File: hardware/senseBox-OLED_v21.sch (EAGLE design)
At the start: 28 parts, among them IC2 VREG-TS9011-3V3, IC4 MAX8XX-809R, J1 JUMPER2-0402-NC, J2 JST4-B4B-PH-SM4-TB, T3 BSS138PS, X1 PASSER-07, X2 PASSER-07, X3 PASSER-07, X4 PASSER-07

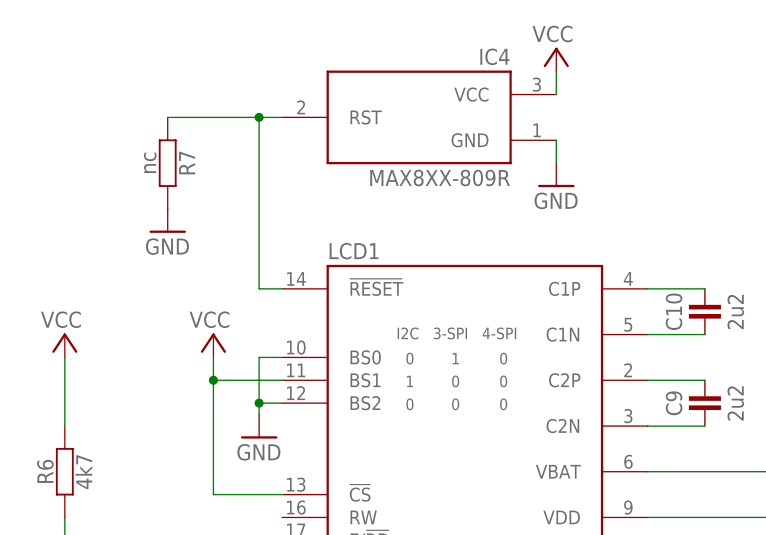
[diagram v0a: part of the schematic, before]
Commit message: updated schematics
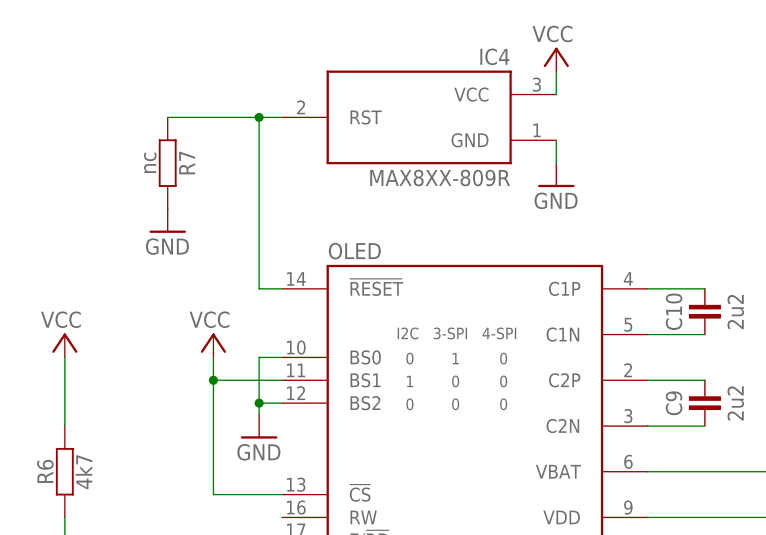
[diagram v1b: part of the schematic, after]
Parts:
- renumbered LCD1 to OLED
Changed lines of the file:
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@@
 <part name="C4" library="we-rcl" deviceset="CAPACITOR" device="-0402" value="100n"/>
 <part name="C1" library="we-rcl" deviceset="CAPACITOR" device="-0402" value="100n"/>
-<part name="LCD1" library="we-opto" deviceset="UG2864HSWEG01" device="-B"/>
+<part name="OLED" library="we-opto" deviceset="UG2864HSWEG01" device="-B"/>
 <part name="GND7" library="supply1" deviceset="GND" device=""/>
 <part name="R6" library="we-rcl" deviceset="RESISTOR" device="-0402" value="4k7"/>
@@
 <instance part="C4" gate="C" x="139.7" y="19.05" rot="R90"/>
 <instance part="C1" gate="C" x="86.36" y="19.05" rot="R90"/>
-<instance part="LCD1" gate="LCD" x="113.03" y="111.76"/>
+<instance part="OLED" gate="LCD" x="113.03" y="111.76"/>
 <instance part="GND7" gate="1" x="90.17" y="120.65"/>
 <instance part="R6" gate="R" x="68.58" y="116.84" rot="R90"/>
@@
 </segment>
 <segment>
-<pinref part="LCD1" gate="LCD" pin="BS2"/>
+<pinref part="OLED" gate="LCD" pin="BS2"/>
 <wire x1="92.71" y1="124.46" x2="90.17" y2="124.46" width="0.1524" layer="91"/>
 <wire x1="92.71" y1="129.54" x2="90.17" y2="129.54" width="0.1524" layer="91"/>
@@
 <wire x1="90.17" y1="124.46" x2="90.17" y2="123.19" width="0.1524" layer="91"/>
 <junction x="90.17" y="124.46"/>
-<pinref part="LCD1" gate="LCD" pin="BS0"/>
+<pinref part="OLED" gate="LCD" pin="BS0"/>
 </segment>
 <segment>
@@
 </segment>
 <segment>
-<pinref part="LCD1" gate="LCD" pin="AGND"/>
-<pinref part="LCD1" gate="LCD" pin="GND@3"/>
+<pinref part="OLED" gate="LCD" pin="AGND"/>
+<pinref part="OLED" gate="LCD" pin="GND@3"/>
 <wire x1="133.35" y1="83.82" x2="133.35" y2="86.36" width="0.1524" layer="91"/>
-<pinref part="LCD1" gate="LCD" pin="GND@2"/>
+<pinref part="OLED" gate="LCD" pin="GND@2"/>
 <wire x1="133.35" y1="86.36" x2="133.35" y2="88.9" width="0.1524" layer="91"/>
 <junction x="133.35" y="86.36"/>
-<pinref part="LCD1" gate="LCD" pin="GND@1"/>
+<pinref part="OLED" gate="LCD" pin="GND@1"/>
 <wire x1="133.35" y1="88.9" x2="133.35" y2="91.44" width="0.1524" layer="91"/>
 <junction x="133.35" y="88.9"/>
@@
 </segment>
 <segment>
-<pinref part="LCD1" gate="LCD" pin="!CS"/>
+<pinref part="OLED" gate="LCD" pin="!CS"/>
 <wire x1="92.71" y1="114.3" x2="85.09" y2="114.3" width="0.1524" layer="91"/>
 <wire x1="85.09" y1="114.3" x2="85.09" y2="127" width="0.1524" layer="91"/>
-<pinref part="LCD1" gate="LCD" pin="BS1"/>
+<pinref part="OLED" gate="LCD" pin="BS1"/>
 <wire x1="85.09" y1="127" x2="85.09" y2="129.54" width="0.1524" layer="91"/>
 <wire x1="92.71" y1="127" x2="85.09" y2="127" width="0.1524" layer="91"/>
@@
 </segment>
 <segment>
-<pinref part="LCD1" gate="LCD" pin="VBAT"/>
+<pinref part="OLED" gate="LCD" pin="VBAT"/>
 <pinref part="P+2" gate="VCC" pin="VCC"/>
 <wire x1="133.35" y1="116.84" x2="158.75" y2="116.84" width="0.1524" layer="91"/>
@@
 <wire x1="165.1" y1="97.79" x2="165.1" y2="116.84" width="0.1524" layer="91"/>
 <junction x="165.1" y="116.84"/>
-<pinref part="LCD1" gate="LCD" pin="VDD"/>
+<pinref part="OLED" gate="LCD" pin="VDD"/>
 <pinref part="C7" gate="C" pin="2"/>
 <wire x1="133.35" y1="111.76" x2="158.75" y2="111.76" width="0.1524" layer="91"/>
@@
 <wire x1="90.17" y1="99.06" x2="85.09" y2="99.06" width="0.1524" layer="91"/>
 <label x="85.09" y="99.06" size="1.27" layer="95" rot="R180" xref="yes"/>
-<pinref part="LCD1" gate="LCD" pin="D2/SDA"/>
+<pinref part="OLED" gate="LCD" pin="D2/SDA"/>
 <wire x1="92.71" y1="96.52" x2="90.17" y2="96.52" width="0.1524" layer="91"/>
 <wire x1="90.17" y1="96.52" x2="90.17" y2="99.06" width="0.1524" layer="91"/>
-<pinref part="LCD1" gate="LCD" pin="D1/DIN/SDA"/>
+<pinref part="OLED" gate="LCD" pin="D1/DIN/SDA"/>
 <wire x1="90.17" y1="99.06" x2="92.71" y2="99.06" width="0.1524" layer="91"/>
 <junction x="90.17" y="99.06"/>
@@
 <wire x1="92.71" y1="101.6" x2="85.09" y2="101.6" width="0.1524" layer="91"/>
 <label x="85.09" y="101.6" size="1.27" layer="95" rot="R180" xref="yes"/>
-<pinref part="LCD1" gate="LCD" pin="D0/SCK"/>
+<pinref part="OLED" gate="LCD" pin="D0/SCK"/>
 </segment>
 </net>
 <net name="SA0" class="0">
 <segment>
-<pinref part="LCD1" gate="LCD" pin="DC/I2C_SA0"/>
+<pinref part="OLED" gate="LCD" pin="DC/I2C_SA0"/>
 <wire x1="92.71" y1="106.68" x2="68.58" y2="106.68" width="0.1524" layer="91"/>
 <wire x1="68.58" y1="106.68" x2="68.58" y2="111.76" width="0.1524" layer="91"/>
@@
 <net name="C2N" class="0">
 <segment>
-<pinref part="LCD1" gate="LCD" pin="C2N"/>
+<pinref part="OLED" gate="LCD" pin="C2N"/>
 <wire x1="133.35" y1="121.92" x2="139.7" y2="121.92" width="0.1524" layer="91"/>
 <pinref part="C9" gate="C" pin="1"/>
@@
 <net name="C2P" class="0">
 <segment>
-<pinref part="LCD1" gate="LCD" pin="C2P"/>
+<pinref part="OLED" gate="LCD" pin="C2P"/>
 <wire x1="133.35" y1="127" x2="139.7" y2="127" width="0.1524" layer="91"/>
 <pinref part="C9" gate="C" pin="2"/>
@@
 <net name="C1N" class="0">
 <segment>
-<pinref part="LCD1" gate="LCD" pin="C1N"/>
+<pinref part="OLED" gate="LCD" pin="C1N"/>
 <wire x1="133.35" y1="132.08" x2="139.7" y2="132.08" width="0.1524" layer="91"/>
 <pinref part="C10" gate="C" pin="1"/>
@@
 <net name="C1P" class="0">
 <segment>
-<pinref part="LCD1" gate="LCD" pin="C1P"/>
+<pinref part="OLED" gate="LCD" pin="C1P"/>
 <wire x1="133.35" y1="137.16" x2="139.7" y2="137.16" width="0.1524" layer="91"/>
 <pinref part="C10" gate="C" pin="2"/>
@@
 <net name="IREF" class="0">
 <segment>
-<pinref part="LCD1" gate="LCD" pin="IREF"/>
+<pinref part="OLED" gate="LCD" pin="IREF"/>
 <pinref part="R5" gate="R" pin="1"/>
 <wire x1="138.43" y1="96.52" x2="133.35" y2="96.52" width="0.1524" layer="91"/>
@@
 <net name="VCH" class="0">
 <segment>
-<pinref part="LCD1" gate="LCD" pin="VCOMH"/>
+<pinref part="OLED" gate="LCD" pin="VCOMH"/>
 <pinref part="C5" gate="C" pin="2"/>
 <wire x1="133.35" y1="101.6" x2="146.05" y2="101.6" width="0.1524" layer="91"/>
@@
 <net name="VC" class="0">
 <segment>
-<pinref part="LCD1" gate="LCD" pin="VCC"/>
+<pinref part="OLED" gate="LCD" pin="VCC"/>
 <pinref part="C6" gate="C" pin="2"/>
 <wire x1="133.35" y1="106.68" x2="152.4" y2="106.68" width="0.1524" layer="91"/>
@@
 <net name="RST" class="0">
 <segment>
-<pinref part="LCD1" gate="LCD" pin="!RESET"/>
+<pinref part="OLED" gate="LCD" pin="!RESET"/>
 <wire x1="92.71" y1="137.16" x2="90.17" y2="137.16" width="0.1524" layer="91"/>
 <wire x1="90.17" y1="137.16" x2="90.17" y2="156.21" width="0.1524" layer="91"/>
